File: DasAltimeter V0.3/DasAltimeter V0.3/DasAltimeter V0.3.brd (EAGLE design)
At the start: 38.9 x 21.6 mm, 55 parts, among them IC1 BMI055, U1 ATSAMD21G-A, U2 3.3V/150mA, U3 MS5803-14BA, U5 ADXL377, X1 22-23-2041, X2 22-23-2041

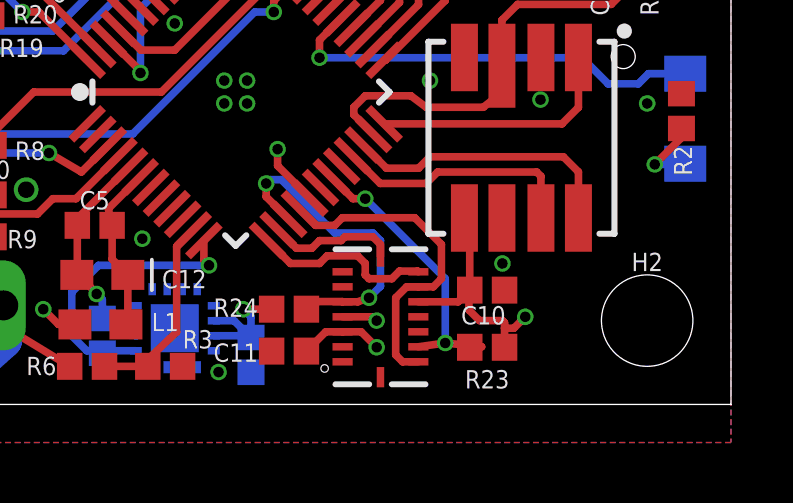
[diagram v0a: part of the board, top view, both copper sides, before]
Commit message: Das Altimeter V0.3 assembled and working!
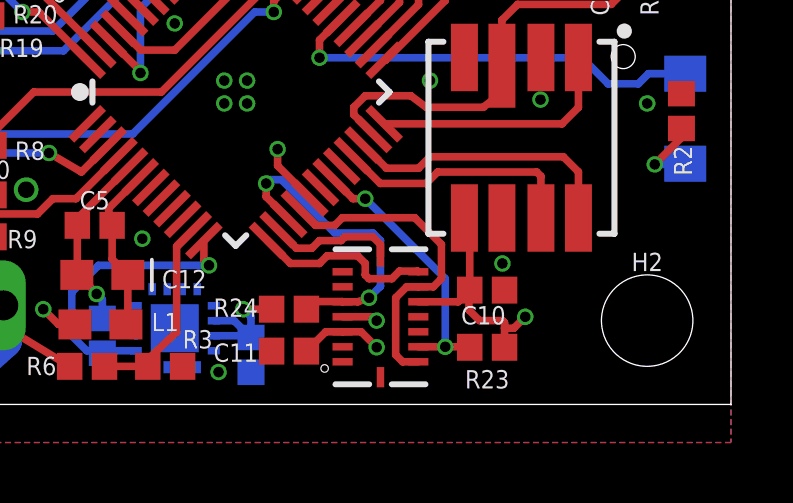
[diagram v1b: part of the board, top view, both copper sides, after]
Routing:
- net CS_ACCEL: track 9.88 -> 9.23 mm
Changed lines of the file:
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@@
 <contactref element="R23" pad="2"/>
 <contactref element="U1" pad="19"/>
-<wire x1="27.36" y1="-0.889" x2="27.757" y2="-0.873" width="0.254" layer="1"/>
-<wire x1="27.757" y1="-0.873" x2="26.543" y2="-0.746" width="0.254" layer="1"/>
-<wire x1="26.543" y1="-0.746" x2="25.6465" y2="-0.873" width="0.254" layer="1"/>
+<wire x1="27.36" y1="-0.889" x2="27.376" y2="-0.873" width="0.254" layer="1"/>
+<wire x1="27.376" y1="-0.873" x2="26.543" y2="-0.873" width="0.254" layer="1"/>
+<wire x1="26.543" y1="-0.873" x2="25.6465" y2="-0.873" width="0.254" layer="1"/>
 <wire x1="22.739978125" y1="4.791571875" x2="23.46755" y2="4.064" width="0.254" layer="1"/>
 <wire x1="23.46755" y1="4.064" x2="23.876" y2="4.064" width="0.254" layer="1"/>
 <via x="23.876" y="4.064" extent="1-16" drill="0.35"/>
 <wire x1="23.876" y1="4.064" x2="26.543" y2="1.397" width="0.254" layer="16"/>
-<via x="26.543" y="-0.746" extent="1-16" drill="0.35"/>
-<wire x1="26.543" y1="1.397" x2="26.543" y2="-0.746" width="0.254" layer="16"/>
+<via x="26.543" y="-0.873" extent="1-16" drill="0.35"/>
+<wire x1="26.543" y1="1.397" x2="26.543" y2="-0.873" width="0.254" layer="16"/>
 </signal>
 <signal name="SPI0_MOSI">
